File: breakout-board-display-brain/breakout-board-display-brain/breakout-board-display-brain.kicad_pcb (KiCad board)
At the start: 2 copper layers, 0 parts

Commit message: further work on breakout board display brain
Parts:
- added J1: Conn_01x15_Socket, Connector_PinSocket_2.54mm:PinSocket_1x15_P2.54mm_Vertical, F.Cu at (141.1, 69.4)
- added J2: Conn_01x15_Socket, Connector_PinSocket_2.54mm:PinSocket_1x15_P2.54mm_Vertical, F.Cu at (162.8, 104.9)
- added J3: Conn_01x16_Female, Connector_PinSocket_2.54mm:PinSocket_1x16_P2.54mm_Vertical, F.Cu at (132.3, 69.5)
- added RV1: R_Potentiometer, Potentiometer_THT:Potentiometer_ACP_CA9-V10_Vertical, F.Cu at (184.0, 88.3)
- added SW1: RotaryEncoder_Switch, Rotary_Encoder:RotaryEncoder_Alps_EC11E-Switch_Vertical_H20mm, F.Cu at (169.3, 72.3)
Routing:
- net GND: track 0.00 -> 94.5 mm
- net /5V: track 0.00 -> 9.88 mm

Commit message: brbrain
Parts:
- moved SW1 55.2 mm to (145.2, 122.0)
- moved RV1 48.0 mm to (157.4, 48.3)
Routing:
- net /Pin_3: track 0.00 -> 146.4 mm
- net /Pin_2: track 0.00 -> 129.3 mm
- net /Pin_1: track 0.00 -> 115.8 mm
- net /Pin_0: track 0.00 -> 99.0 mm
- net /5V: track 9.88 -> 99.0 mm
- net /Pin_9: track 0.00 -> 78.3 mm
- net /Pin_8: track 0.00 -> 42.0 mm
- net /Pin_7: track 0.00 -> 42.0 mm
- net /V0: track 0.00 -> 35.5 mm
- net /Pin_4: track 0.00 -> 20.0 mm
- net /Pin_5: track 0.00 -> 19.7 mm
- net /Pin_6: track 0.00 -> 18.9 mm
- net GND: track 94.5 -> 84.0 mm
- added copper zone on B.Cu, net (none)

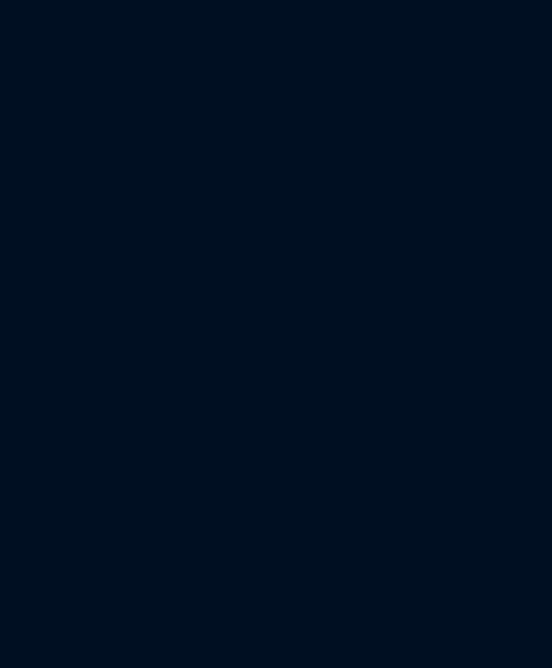
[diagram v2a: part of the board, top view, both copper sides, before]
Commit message: connector added to display-brain breakout board
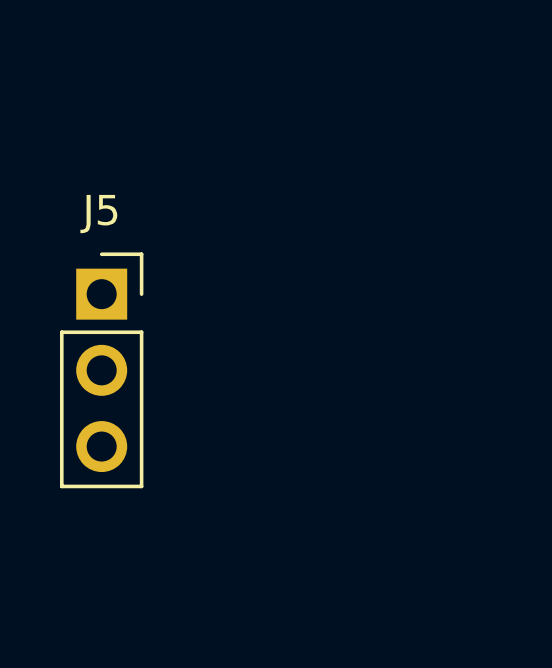
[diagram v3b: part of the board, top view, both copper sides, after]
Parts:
- added J5: Conn_01x03_Socket, Connector_PinSocket_2.54mm:PinSocket_1x03_P2.54mm_Vertical, F.Cu at (103.4, 75.5)
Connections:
- net /3.3V renamed +3.3V
- net /5V renamed +5V
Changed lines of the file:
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@@
   (net 0 "")
   (net 1 "GND")
-  (net 2 "/3.3V")
+  (net 2 "+3.3V")
   (net 3 "/RST")
   (net 4 "/Pin_4")
@@
   (net 8 "/Pin_8")
   (net 9 "/Pin_9")
-  (net 10 "/5V")
+  (net 10 "+5V")
   (net 11 "/Pin_19")
   (net 12 "/Pin_18")
@@
       (net 20 "/V0") (pinfunction "2") (pintype "passive"))
     (pad "3" thru_hole circle (at 0 -5 180) (size 2.34 2.34) (drill 1.3) (layers "*.Cu" "*.Mask")
-      (net 10 "/5V") (pinfunction "3") (pintype "passive"))
+      (net 10 "+5V") (pinfunction "3") (pintype "passive"))
     (model "${KICAD6_3DMODEL_DIR}/Potentiometer_THT.3dshapes/Potentiometer_ACP_CA9-V10_Vertical.wrl"
+      (offset (xyz 0 0 0))
+      (scale (xyz 1 1 1))
+      (rotate (xyz 0 0 0))
+    )
+  )
+  (footprint "Connector_PinSocket_2.54mm:PinSocket_1x03_P2.54mm_Vertical" (layer "F.Cu")
+    (at 103.4 75.52)
+    (descr "Through hole straight socket strip, 1x03, 2.54mm pitch, single row (from Kicad 4.0.7), script generated")
+    (tags "Through hole socket strip THT 1x03 2.54mm single row")
+    (property "Sheetfile" "breakout-board-display-brain.kicad_sch")
+    (property "Sheetname" "")
+    (property "ki_description" "Generic connector, single row, 01x03, script generated")
+    (property "ki_keywords" "connector")
+    (attr through_hole)
+    (fp_text reference "J5" (at 0 -2.77) (layer "F.SilkS")
+        (effects (font (size 1 1) (thickness 0.15)))
+    )
+    (fp_text value "Conn_01x03_Socket" (at 0 7.85) (layer "F.Fab")
+        (effects (font (size 1 1) (thickness 0.15)))
+    )
+    (fp_text user "${REFERENCE}" (at 0 2.54 90) (layer "F.Fab")
+        (effects (font (size 1 1) (thickness 0.15)))
+    )
+    (fp_line (start -1.33 1.27) (end -1.33 6.41)
+      (stroke (width 0.12) (type solid)) (layer "F.SilkS"))
+    (fp_line (start -1.33 1.27) (end 1.33 1.27)
+      (stroke (width 0.12) (type solid)) (layer "F.SilkS"))
+    (fp_line (start -1.33 6.41) (end 1.33 6.41)
+      (stroke (width 0.12) (type solid)) (layer "F.SilkS"))
+    (fp_line (start 0 -1.33) (end 1.33 -1.33)
+      (stroke (width 0.12) (type solid)) (layer "F.SilkS"))
+    (fp_line (start 1.33 -1.33) (end 1.33 0)
+      (stroke (width 0.12) (type solid)) (layer "F.SilkS"))
+    (fp_line (start 1.33 1.27) (end 1.33 6.41)
+      (stroke (width 0.12) (type solid)) (layer "F.SilkS"))
+    (fp_line (start -1.8 -1.8) (end 1.75 -1.8)
+      (stroke (width 0.05) (type solid)) (layer "F.CrtYd"))
+    (fp_line (start -1.8 6.85) (end -1.8 -1.8)
+      (stroke (width 0.05) (type solid)) (layer "F.CrtYd"))
+    (fp_line (start 1.75 -1.8) (end 1.75 6.85)
+      (stroke (width 0.05) (type solid)) (layer "F.CrtYd"))
+    (fp_line (start 1.75 6.85) (end -1.8 6.85)
+      (stroke (width 0.05) (type solid)) (layer "F.CrtYd"))
+    (fp_line (start -1.27 -1.27) (end 0.635 -1.27)
+      (stroke (width 0.1) (type solid)) (layer "F.Fab"))
+    (fp_line (start -1.27 6.35) (end -1.27 -1.27)
+      (stroke (width 0.1) (type solid)) (layer "F.Fab"))
+    (fp_line (start 0.635 -1.27) (end 1.27 -0.635)
+      (stroke (width 0.1) (type solid)) (layer "F.Fab"))
+    (fp_line (start 1.27 -0.635) (end 1.27 6.35)
+      (stroke (width 0.1) (type solid)) (layer "F.Fab"))
+    (fp_line (start 1.27 6.35) (end -1.27 6.35)
+      (stroke (width 0.1) (type solid)) (layer "F.Fab"))
+    (pad "1" thru_hole rect (at 0 0) (size 1.7 1.7) (drill 1) (layers "*.Cu" "*.Mask")
+      (net 10 "+5V") (pinfunction "Pin_1") (pintype "passive"))
+    (pad "2" thru_hole oval (at 0 2.54) (size 1.7 1.7) (drill 1) (layers "*.Cu" "*.Mask")
+      (net 2 "+3.3V") (pinfunction "Pin_2") (pintype "passive"))
+    (pad "3" thru_hole oval (at 0 5.08) (size 1.7 1.7) (drill 1) (layers "*.Cu" "*.Mask")
+      (net 1 "GND") (pinfunction "Pin_3") (pintype "passive"))
+    (model "${KICAD6_3DMODEL_DIR}/Connector_PinSocket_2.54mm.3dshapes/PinSocket_1x03_P2.54mm_Vertical.wrl"
       (offset (xyz 0 0 0))
       (scale (xyz 1 1 1))
@@
       (net 1 "GND") (pinfunction "Pin_1") (pintype "passive"))
     (pad "2" thru_hole oval (at 0 2.54) (size 1.7 1.7) (drill 1) (layers "*.Cu" "*.Mask")
-      (net 2 "/3.3V") (pinfunction "Pin_2") (pintype "passive"))
+      (net 2 "+3.3V") (pinfunction "Pin_2") (pintype "passive"))
     (pad "3" thru_hole oval (at 0 5.08) (size 1.7 1.7) (drill 1) (layers "*.Cu" "*.Mask")
-      (net 2 "/3.3V") (pinfunction "Pin_3") (pintype "passive"))
+      (net 2 "+3.3V") (pinfunction "Pin_3") (pintype "passive"))
     (pad "4" thru_hole oval (at 0 7.62) (size 1.7 1.7) (drill 1) (layers "*.Cu" "*.Mask")
       (net 3 "/RST") (pinfunction "Pin_4") (pintype "passive+no_connect"))
@@
       (net 6 "/Pin_6") (pinfunction "Pin_8") (pintype "passive"))
     (pad "9" thru_hole oval (at 0 20.32) (size 1.7 1.7) (drill 1) (layers "*.Cu" "*.Mask")
-      (net 7 "/Pin_7") (pinfunction "Pin_9") (pintype "passive"))
+      (net 7 "/Pin_7") (pinfunction "Pin_9") (pintype "passive+no_connect"))
     (pad "10" thru_hole oval (at 0 22.86) (size 1.7 1.7) (drill 1) (layers "*.Cu" "*.Mask")
       (net 1 "GND") (pinfunction "Pin_10") (pintype "passive"))
     (pad "11" thru_hole oval (at 0 25.4) (size 1.7 1.7) (drill 1) (layers "*.Cu" "*.Mask")
-      (net 8 "/Pin_8") (pinfunction "Pin_11") (pintype "passive"))
+      (net 8 "/Pin_8") (pinfunction "Pin_11") (pintype "passive+no_connect"))
     (pad "12" thru_hole oval (at 0 27.94) (size 1.7 1.7) (drill 1) (layers "*.Cu" "*.Mask")
       (net 9 "/Pin_9") (pinfunction "Pin_12") (pintype "passive"))
     (pad "13" thru_hole oval (at 0 30.48) (size 1.7 1.7) (drill 1) (layers "*.Cu" "*.Mask")
-      (net 10 "/5V") (pinfunction "Pin_13") (pintype "passive"))
+      (net 10 "+5V") (pinfunction "Pin_13") (pintype "passive"))
     (pad "14" thru_hole oval (at 0 33.02) (size 1.7 1.7) (drill 1) (layers "*.Cu" "*.Mask")
-      (net 10 "/5V") (pinfunction "Pin_14") (pintype "passive"))
+      (net 10 "+5V") (pinfunction "Pin_14") (pintype "passive"))
     (pad "15" thru_hole oval (at 0 35.56) (size 1.7 1.7) (drill 1) (layers "*.Cu" "*.Mask")
       (net 1 "GND") (pinfunction "Pin_15") (pintype "passive"))
@@
       (net 1 "GND") (pinfunction "Pin_1") (pintype "passive"))
     (pad "2" thru_hole oval (at 0 2.54) (size 1.7 1.7) (drill 1) (layers "*.Cu" "*.Mask")
-      (net 10 "/5V") (pinfunction "Pin_2") (pintype "passive"))
+      (net 10 "+5V") (pinfunction "Pin_2") (pintype "passive"))
     (pad "3" thru_hole oval (at 0 5.08) (size 1.7 1.7) (drill 1) (layers "*.Cu" "*.Mask")
       (net 20 "/V0") (pinfunction "Pin_3") (pintype "passive"))
@@
       (net 6 "/Pin_6") (pinfunction "Pin_14") (pintype "passive"))
     (pad "15" thru_hole oval (at 0 35.56) (size 1.7 1.7) (drill 1) (layers "*.Cu" "*.Mask")
-      (net 10 "/5V") (pinfunction "Pin_15") (pintype "passive"))
+      (net 10 "+5V") (pinfunction "Pin_15") (pintype "passive"))
     (pad "16" thru_hole oval (at 0 38.1) (size 1.7 1.7) (drill 1) (layers "*.Cu" "*.Mask")
       (net 1 "GND") (pinfunction "Pin_16") (pintype "passive"))
@@
       (stroke (width 0.12) (type solid)) (fill none) (layer "F.Fab"))
     (pad "A" thru_hole rect (at 0 0) (size 2 2) (drill 1) (layers "*.Cu" "*.Mask")
-      (net 7 "/Pin_7") (pinfunction "A") (pintype "passive"))
+      (net 7 "/Pin_7") (pinfunction "A") (pintype "passive+no_connect"))
     (pad "B" thru_hole circle (at 0 5) (size 2 2) (drill 1) (layers "*.Cu" "*.Mask")
-      (net 8 "/Pin_8") (pinfunction "B") (pintype "passive"))
+      (net 8 "/Pin_8") (pinfunction "B") (pintype "passive+no_connect"))
     (pad "C" thru_hole circle (at 0 2.5) (size 2 2) (drill 1) (layers "*.Cu" "*.Mask")
       (net 1 "GND") (pinfunction "C") (pintype "passive"))

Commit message: Routing
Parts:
- removed J5: Conn_01x03_Socket, Connector_PinSocket_2.54mm:PinSocket_1x03_P2.54mm_Vertical
- added J4: Conn_01x02_Socket, Connector_PinSocket_2.54mm:PinSocket_1x02_P2.54mm_Vertical, F.Cu at (138.7, 66.1)
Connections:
- net +3.3V renamed /3.3V
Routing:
- net /Pin_3: track 146.4 -> 137.0 mm
- net GND: track 84.0 -> 90.5 mm
- net +5V: track 99.0 -> 103.4 mm
